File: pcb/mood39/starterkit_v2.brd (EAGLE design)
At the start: 32 x 32 mm, 18 parts, among them IC1 TINY85, IC2 LM2940, X1 PWRUSB

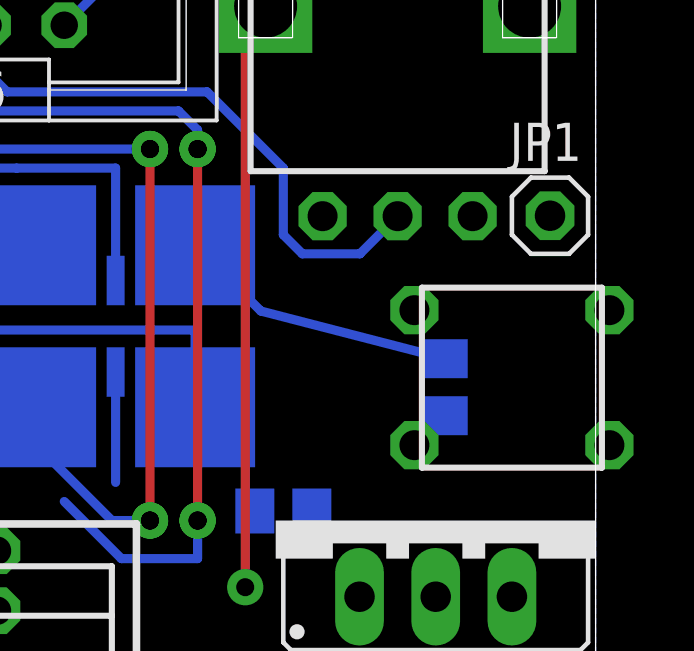
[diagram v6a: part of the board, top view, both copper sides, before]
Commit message: add pins for USB data
those pins can be used for actually accessing the avr via USB, but it
needs some additional circuit stacked on the pin headers
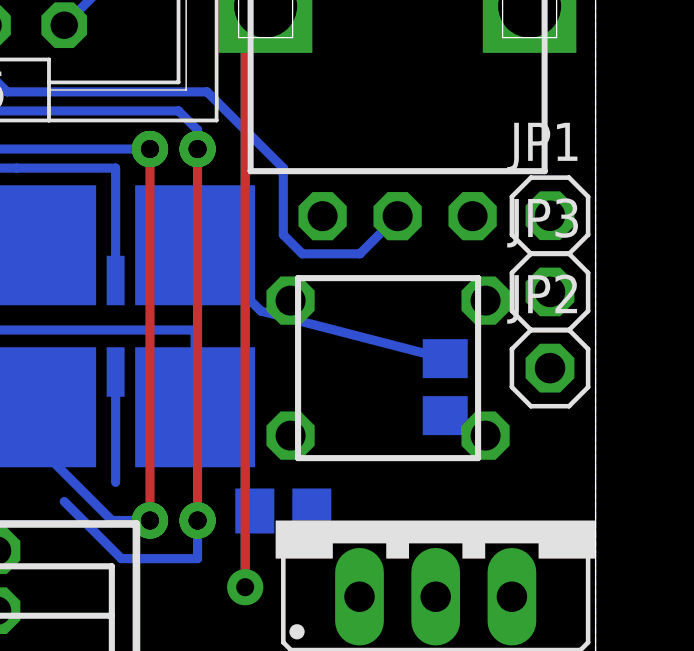
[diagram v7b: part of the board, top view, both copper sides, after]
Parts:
- added JP2, JP3: (no value), pinhead:1X01
- moved S1 4.14 mm to (25.1, 14.6)
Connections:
- net USBD+: now also JP2.1
- net USBD-: now also JP3.1
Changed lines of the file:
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@@
 <?xml version="1.0" encoding="utf-8"?>
 <!DOCTYPE eagle SYSTEM "eagle.dtd">
-<eagle version="6.4">
+<eagle version="6.5.0">
 <drawing>
 <settings>
@@
 <element name="LED2" library="led" package="LED3MM" value="rot lc" x="2.54" y="6.6675" rot="R270"/>
 <element name="R6" library="rcl" package="R0805" value="1.5k" x="2.8575" y="9.8425" rot="MR0"/>
-<element name="S1" library="n39" package="JTP-1130" value="" x="29.21" y="14.2875">
-<attribute name="REICHELT" value="TASTER 9305" x="29.21" y="14.2875" size="1.778" layer="27" display="off"/>
+<element name="S1" library="n39" package="JTP-1130" value="" x="25.0825" y="14.605">
+<attribute name="REICHELT" value="TASTER 9305" x="25.0825" y="14.605" size="1.778" layer="27" display="off"/>
 </element>
 <element name="U$1" library="n39" package="RIACON_101_2" value="RIACON_101_2" x="10.795" y="3.81">
 <attribute name="REICHELT" value="AKL 101-02" x="10.795" y="3.81" size="1.778" layer="27" display="off"/>
 </element>
+<element name="JP2" library="pinhead" package="1X01" value="" x="30.48" y="14.605"/>
+<element name="JP3" library="pinhead" package="1X01" value="" x="30.48" y="17.145"/>
 </elements>
 <signals>
@@
 <contactref element="U$1" pad="1"/>
 <wire x1="26.9875" y1="13.02" x2="27.9" y2="19.67" width="0" layer="19" extent="16-16"/>
-<wire x1="25.96" y1="12.0375" x2="26.9875" y2="13.02" width="0" layer="19" extent="16-16"/>
-<wire x1="22.54" y1="9.8425" x2="25.96" y2="12.0375" width="0" layer="19" extent="16-16"/>
+<wire x1="21.8325" y1="12.355" x2="26.9875" y2="13.02" width="0" layer="19" extent="16-16"/>
+<wire x1="22.54" y1="9.8425" x2="21.8325" y2="12.355" width="0" layer="19" extent="16-16"/>
 <wire x1="26.67" y1="6.985" x2="22.54" y2="9.8425" width="0" layer="19" extent="16-16"/>
 <wire x1="24.13" y1="2.54" x2="26.67" y2="6.985" width="0" layer="19" extent="1-1"/>
 <wire x1="21.27" y1="4.1275" x2="24.13" y2="2.54" width="0" layer="19" extent="16-16"/>
-<wire x1="32.46" y1="12.0375" x2="26.9875" y2="13.02" width="0" layer="19" extent="16-16"/>
+<wire x1="28.3325" y1="12.355" x2="26.9875" y2="13.02" width="0" layer="19" extent="16-16"/>
 <wire x1="12.045" y1="6.52" x2="21.27" y2="4.1275" width="0" layer="19" extent="16-16"/>
 <wire x1="8.255" y1="3.81" x2="12.045" y2="6.52" width="0" layer="19" extent="1-1"/>
@@
 <contactref element="S1" pad="3"/>
 <contactref element="S1" pad="4"/>
-<wire x1="32.46" y1="16.5375" x2="30.48" y2="19.685" width="0" layer="19" extent="1-1"/>
-<wire x1="25.96" y1="16.5375" x2="30.48" y2="19.685" width="0" layer="19" extent="1-1"/>
-<wire x1="9.525" y1="12.7" x2="25.96" y2="16.5375" width="0" layer="19" extent="1-1"/>
+<wire x1="28.3325" y1="16.855" x2="30.48" y2="19.685" width="0" layer="19" extent="1-1"/>
+<wire x1="21.8325" y1="16.855" x2="30.48" y2="19.685" width="0" layer="19" extent="1-1"/>
+<wire x1="9.525" y1="12.7" x2="21.8325" y2="16.855" width="0" layer="19" extent="1-1"/>
 <wire x1="11.7475" y1="28.575" x2="11.7475" y2="27.94" width="0.3048" layer="16"/>
 <wire x1="11.7475" y1="27.94" x2="10.4775" y2="26.67" width="0.3048" layer="16"/>
@@
 <signal name="USBD-">
 <contactref element="X1" pad="2"/>
+<contactref element="JP3" pad="1"/>
+<wire x1="30.48" y1="17.145" x2="9.545" y2="8.52" width="0" layer="19" extent="1-1"/>
 </signal>
 <signal name="USBD+">
 <contactref element="X1" pad="3"/>
+<contactref element="JP2" pad="1"/>
+<wire x1="30.48" y1="14.605" x2="9.545" y2="6.52" width="0" layer="19" extent="1-1"/>
 </signal>
 <signal name="V+" class="1">

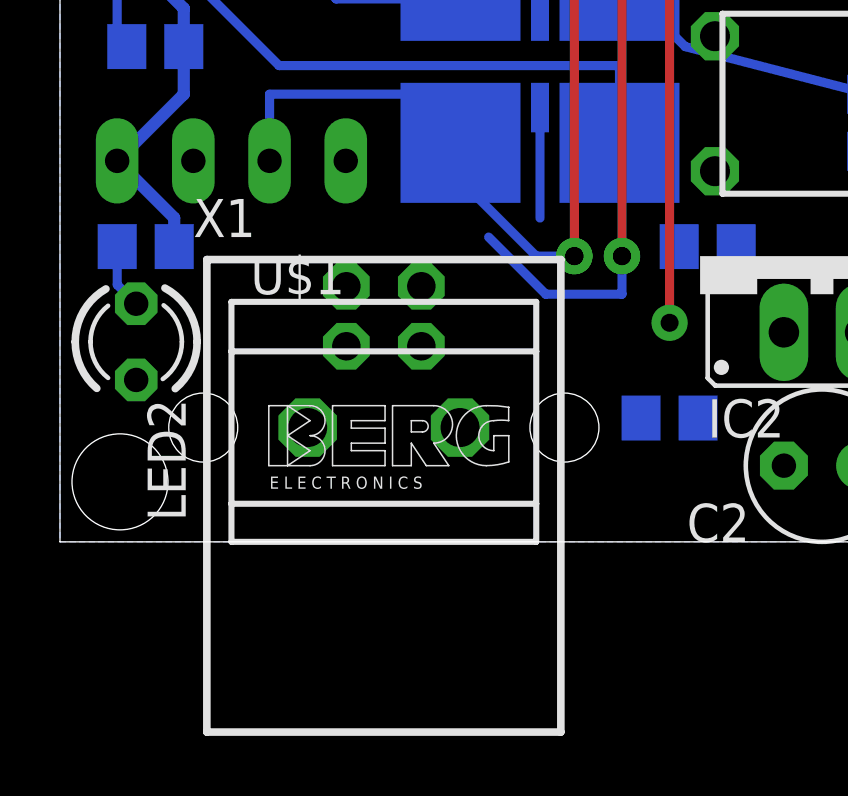
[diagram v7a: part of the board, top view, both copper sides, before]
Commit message: replaced USB connector
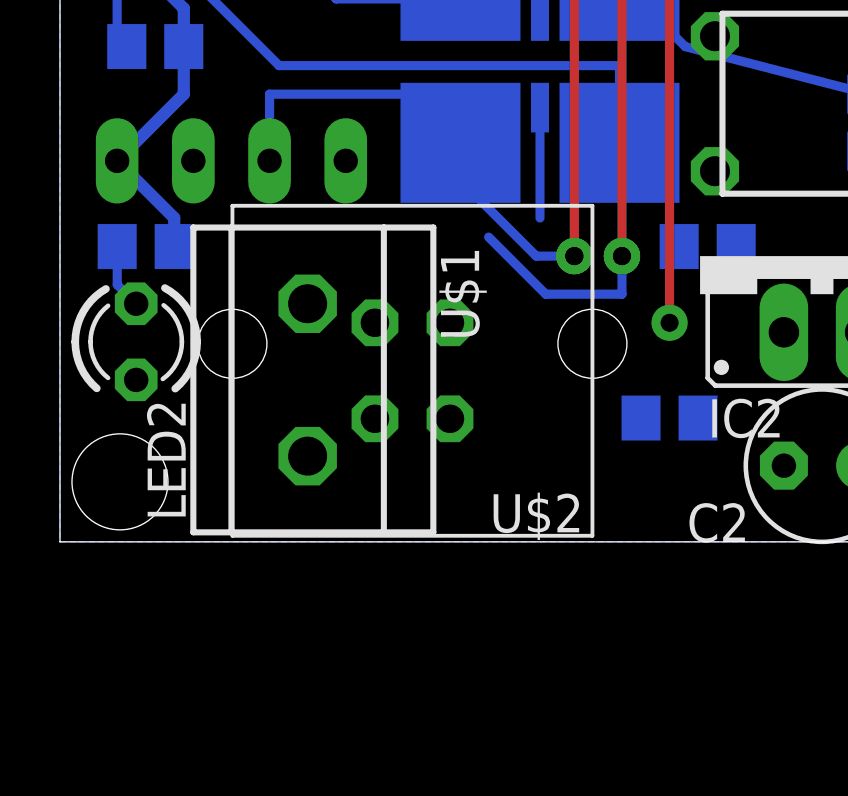
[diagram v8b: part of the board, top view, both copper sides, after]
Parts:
- removed X1: PWRUSB, con-berg:PN61729
- added U$2: USB_B, n39:USB_B_UP
- moved U$1 3.00 mm to (8.26, 5.40), turned to 270 degrees
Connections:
- net GND: now also U$2.4; no longer X1.4
- net USBD+: now also U$2.3; no longer X1.3
- net USBD-: now also U$2.2; no longer X1.2
- net VCC: now also U$2.1; no longer X1.1
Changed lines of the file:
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@@
 <attribute name="OC_FARNELL" value="unknown" x="33.3375" y="0.635" size="1.778" layer="27" display="off"/>
-</element>
-<element name="X1" library="con-berg" package="PN61729" value="PWRUSB" x="10.795" y="3.81">
-<attribute name="OC_NEWARK" value="unknown" x="42.545" y="-7.62" size="1.778" layer="27" display="off"/>
-<attribute name="MPN" value="" x="42.545" y="-7.62" size="1.778" layer="27" display="off"/>
-<attribute name="MF" value="" x="42.545" y="-7.62" size="1.778" layer="27" display="off"/>
-<attribute name="OC_FARNELL" value="unknown" x="42.545" y="-7.62" size="1.778" layer="27" display="off"/>
 </element>
 <element name="IC2" library="v-reg" package="78XXS" value="LM2940" x="26.67" y="9.525"/>
@@
 <attribute name="REICHELT" value="TASTER 9305" x="25.0825" y="14.605" size="1.778" layer="27" display="off"/>
 </element>
-<element name="U$1" library="n39" package="RIACON_101_2" value="RIACON_101_2" x="10.795" y="3.81">
-<attribute name="REICHELT" value="AKL 101-02" x="10.795" y="3.81" size="1.778" layer="27" display="off"/>
+<element name="U$1" library="n39" package="RIACON_101_2" value="RIACON_101_2" x="8.255" y="5.3975" rot="R270">
+<attribute name="REICHELT" value="AKL 101-02" x="8.255" y="5.3975" size="1.778" layer="27" rot="R270" display="off"/>
 </element>
 <element name="JP2" library="pinhead" package="1X01" value="" x="30.48" y="14.605"/>
 <element name="JP3" library="pinhead" package="1X01" value="" x="30.48" y="17.145"/>
+<element name="U$2" library="n39" package="USB_B_UP" value="USB_B" x="11.7475" y="7.3025" rot="R180">
+<attribute name="REICHELT" value="USB BG" x="11.7475" y="7.3025" size="1.778" layer="27" rot="R180" display="off"/>
+</element>
 </elements>
 <signals>
@@
 <contactref element="C3" pad="2"/>
 <contactref element="SV1" pad="6"/>
-<contactref element="X1" pad="4"/>
 <polygon width="0.4064" layer="16" thermals="no">
 <vertex x="0" y="0"/>
@@
 <contactref element="S1" pad="2"/>
 <contactref element="U$1" pad="1"/>
+<contactref element="U$2" pad="4"/>
 <wire x1="26.9875" y1="13.02" x2="27.9" y2="19.67" width="0" layer="19" extent="16-16"/>
+<wire x1="28.3325" y1="12.355" x2="26.9875" y2="13.02" width="0" layer="19" extent="16-16"/>
 <wire x1="21.8325" y1="12.355" x2="26.9875" y2="13.02" width="0" layer="19" extent="16-16"/>
 <wire x1="22.54" y1="9.8425" x2="21.8325" y2="12.355" width="0" layer="19" extent="16-16"/>
@@
 <wire x1="24.13" y1="2.54" x2="26.67" y2="6.985" width="0" layer="19" extent="1-1"/>
 <wire x1="21.27" y1="4.1275" x2="24.13" y2="2.54" width="0" layer="19" extent="16-16"/>
-<wire x1="28.3325" y1="12.355" x2="26.9875" y2="13.02" width="0" layer="19" extent="16-16"/>
-<wire x1="12.045" y1="6.52" x2="21.27" y2="4.1275" width="0" layer="19" extent="16-16"/>
-<wire x1="8.255" y1="3.81" x2="12.045" y2="6.52" width="0" layer="19" extent="1-1"/>
-<wire x1="2.54" y1="5.3975" x2="8.255" y2="3.81" width="0" layer="19" extent="1-1"/>
-<wire x1="9.525" y1="20.32" x2="12.045" y2="6.52" width="0" layer="19" extent="1-1"/>
+<wire x1="8.255" y1="7.9375" x2="21.27" y2="4.1275" width="0" layer="19" extent="16-16"/>
+<wire x1="2.54" y1="5.3975" x2="8.255" y2="7.9375" width="0" layer="19" extent="1-1"/>
+<wire x1="10.4975" y1="7.3025" x2="8.255" y2="7.9375" width="0" layer="19" extent="1-1"/>
+<wire x1="9.525" y1="20.32" x2="21.8325" y2="12.355" width="0" layer="19" extent="1-1"/>
 <wire x1="5.08" y1="24.7625" x2="9.525" y2="20.32" width="0" layer="19" extent="16-16"/>
 <wire x1="7.3025" y1="26.985" x2="5.08" y2="24.7625" width="0" layer="19" extent="16-16"/>
@@
 <contactref element="C2" pad="+"/>
 <contactref element="SV1" pad="2"/>
-<contactref element="X1" pad="1"/>
 <contactref element="R5" pad="1"/>
 <contactref element="R1" pad="1"/>
@@
 <wire x1="3.8075" y1="10.7975" x2="1.905" y2="12.7" width="0.4064" layer="16"/>
 <wire x1="5.08" y1="22.8625" x2="3.175" y2="22.86" width="0.4064" layer="16"/>
+<contactref element="U$2" pad="1"/>
 <wire x1="29.21" y1="6.985" x2="22.9" y2="19.67" width="0" layer="19" extent="1-1"/>
 <wire x1="26.67" y1="2.54" x2="29.21" y2="6.985" width="0" layer="19" extent="1-1"/>
-<wire x1="12.045" y1="8.52" x2="22.9" y2="19.67" width="0" layer="19" extent="1-1"/>
-<wire x1="3.8075" y1="9.8425" x2="12.045" y2="8.52" width="0" layer="19" extent="16-16"/>
+<wire x1="9.2075" y1="28.575" x2="22.9" y2="19.67" width="0" layer="19" extent="1-1"/>
+<wire x1="10.4975" y1="4.1025" x2="3.8075" y2="9.8425" width="0" layer="19" extent="16-16"/>
 </signal>
 <signal name="N$5" class="2">
@@
 </signal>
 <signal name="USBD-">
-<contactref element="X1" pad="2"/>
 <contactref element="JP3" pad="1"/>
-<wire x1="30.48" y1="17.145" x2="9.545" y2="8.52" width="0" layer="19" extent="1-1"/>
+<contactref element="U$2" pad="2"/>
+<wire x1="12.9975" y1="4.1025" x2="30.48" y2="17.145" width="0" layer="19" extent="1-1"/>
 </signal>
 <signal name="USBD+">
-<contactref element="X1" pad="3"/>
 <contactref element="JP2" pad="1"/>
-<wire x1="30.48" y1="14.605" x2="9.545" y2="6.52" width="0" layer="19" extent="1-1"/>
+<contactref element="U$2" pad="3"/>
+<wire x1="12.9975" y1="7.3025" x2="30.48" y2="14.605" width="0" layer="19" extent="1-1"/>
 </signal>
 <signal name="V+" class="1">
@@
 <contactref element="U$1" pad="2"/>
 <wire x1="19.37" y1="4.1275" x2="24.13" y2="6.985" width="0" layer="19" extent="16-16"/>
-<wire x1="13.335" y1="3.81" x2="19.37" y2="4.1275" width="0" layer="19" extent="16-16"/>
+<wire x1="8.255" y1="2.8575" x2="19.37" y2="4.1275" width="0" layer="19" extent="16-16"/>
 </signal>
 <signal name="N$1" class="2">
